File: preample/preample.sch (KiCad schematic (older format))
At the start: 78 parts, among them J1 Conn_01x03, U1 TPS7A39, U2 OP2228UA, U3 OPA228UA, U4 OP2228UA, U5 OPA228UA

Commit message: changed op amps. changed rail voltages. hooked up bypass caps for op amps. additional passives for noise reduction in op amp circuits.
separated the signal grounds. Need to do more research on if that is a
normal thing. Added rca inputs, need to investigate if a simple switch
is enough or if analog mux circuits are needed.
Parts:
- removed C? (x4): 10uF, symbol Device:C_Small
- removed GND? (x4): GND, symbol power:GND
- added AUXGND?: GNDREF, symbol power:GNDREF
- added C17, C18, C?: 100nF, symbol Device:C_Small
- added C24, C35: 10uF, symbol Device:C_Small
- added C26: 10UF, symbol Device:C_Small
- added C27: 20uF, symbol Device:C_Small
- added GND? (x11): GND, symbol power:GND
- added J2: Conn_01x07, symbol Connector_Generic:Conn_01x07
- added J3, J4, J5, J6: Barrel_Jack, symbol Connector:Barrel_Jack
- added R22, R23: 1K, symbol Device:R_Small_US
- added R?: 100R, symbol Device:R_Small_US
- added RV2, RV3: 100K, symbol Device:R_POT_TRIM
- added S1, S2, S4: 4PDT_Switch, symbol preample:4PDT_Switch
- C19, C21, C22: renamed from C?; value 10uF -> 100nF
- R10, R11, R12, R16, R17, R18, R19, R9: value 5K6 -> 560R
- R15, R8: value 5K6 -> 1K
- R3: value 90K9 -> 132K9
- R5: value 100K8 -> 142K9
- RV1: value R_POT_Dual_Separate -> 50K
- U2, U4: value OP2228UA -> OPA2134UA
- U2, U4: value OP2228UA -> OPA2134UA; symbol preample:OP2228UA -> preample:OP2134UA
- U3, U5: value OPA228UA -> OPA134UA; symbol preample:OPA228UA -> preample:OPA134
- renumbered C18 to C20
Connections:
- net labels added: +17V, -17V, AUDIO_A_1_GND, AUDIO_A_1_IN, AUDIO_A_2_GND, AUDIO_A_2_IN, AUDIO_B_1_GND, AUDIO_B_1_IN, AUDIO_B_2_GND, AUDIO_B_2_IN, SIGNAL_GROUND_1, SIGNAL_GROUND_2, TRIM_1A, TRIM_1B, TRIM_2A, TRIM_2B
- net labels removed: +12V, -12V, SIGNAL_GROUND
- wire segments 160 -> 231
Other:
- note added: "1.0"
- note added: "April 2019"
- note added: "DC OFFSET TRIMMERS"
- note added: "INPUT A"
- note added: "INPUT B"
- note added: "OP AMP BYPASS CAPACITORS"
- note added: "OUTPUT TO POWER AMP"
- note added: "Preample preamp"
- note added: "UNREGULATED POWER IN"
- moved on the sheet: C10, C11, C13, C16, C17, C19, C20, C21, C22, C3, C4, C5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

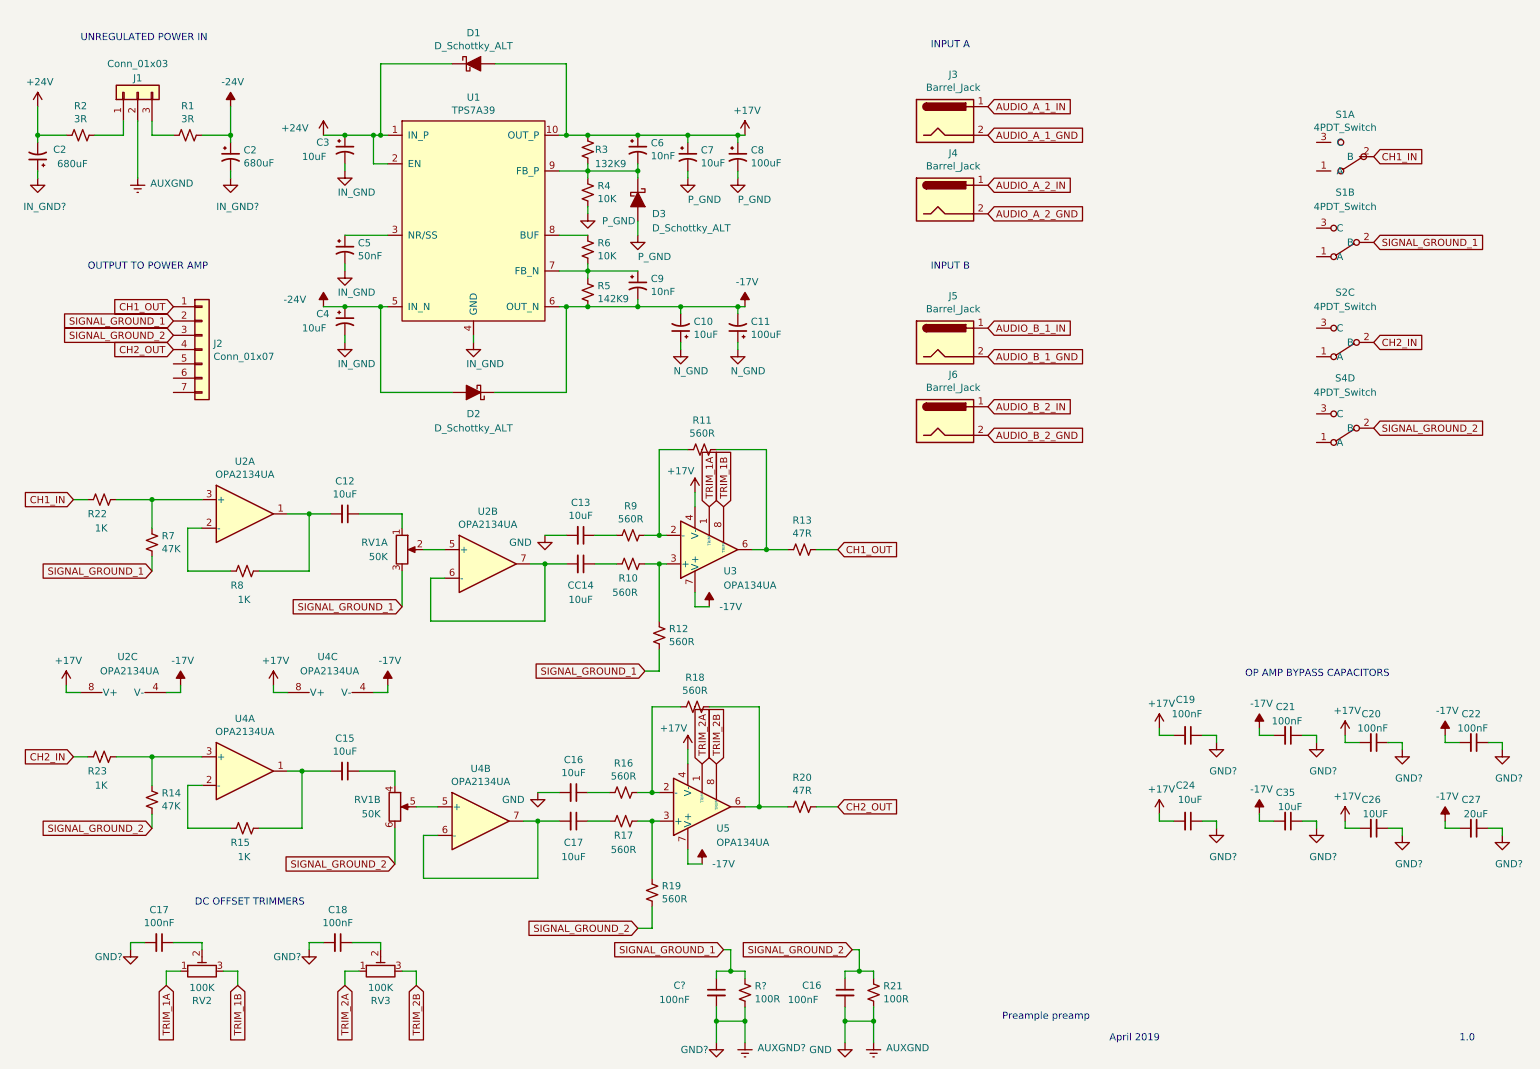
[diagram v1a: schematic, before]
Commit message: added layout sketch. working on grounds. playing with connectors.
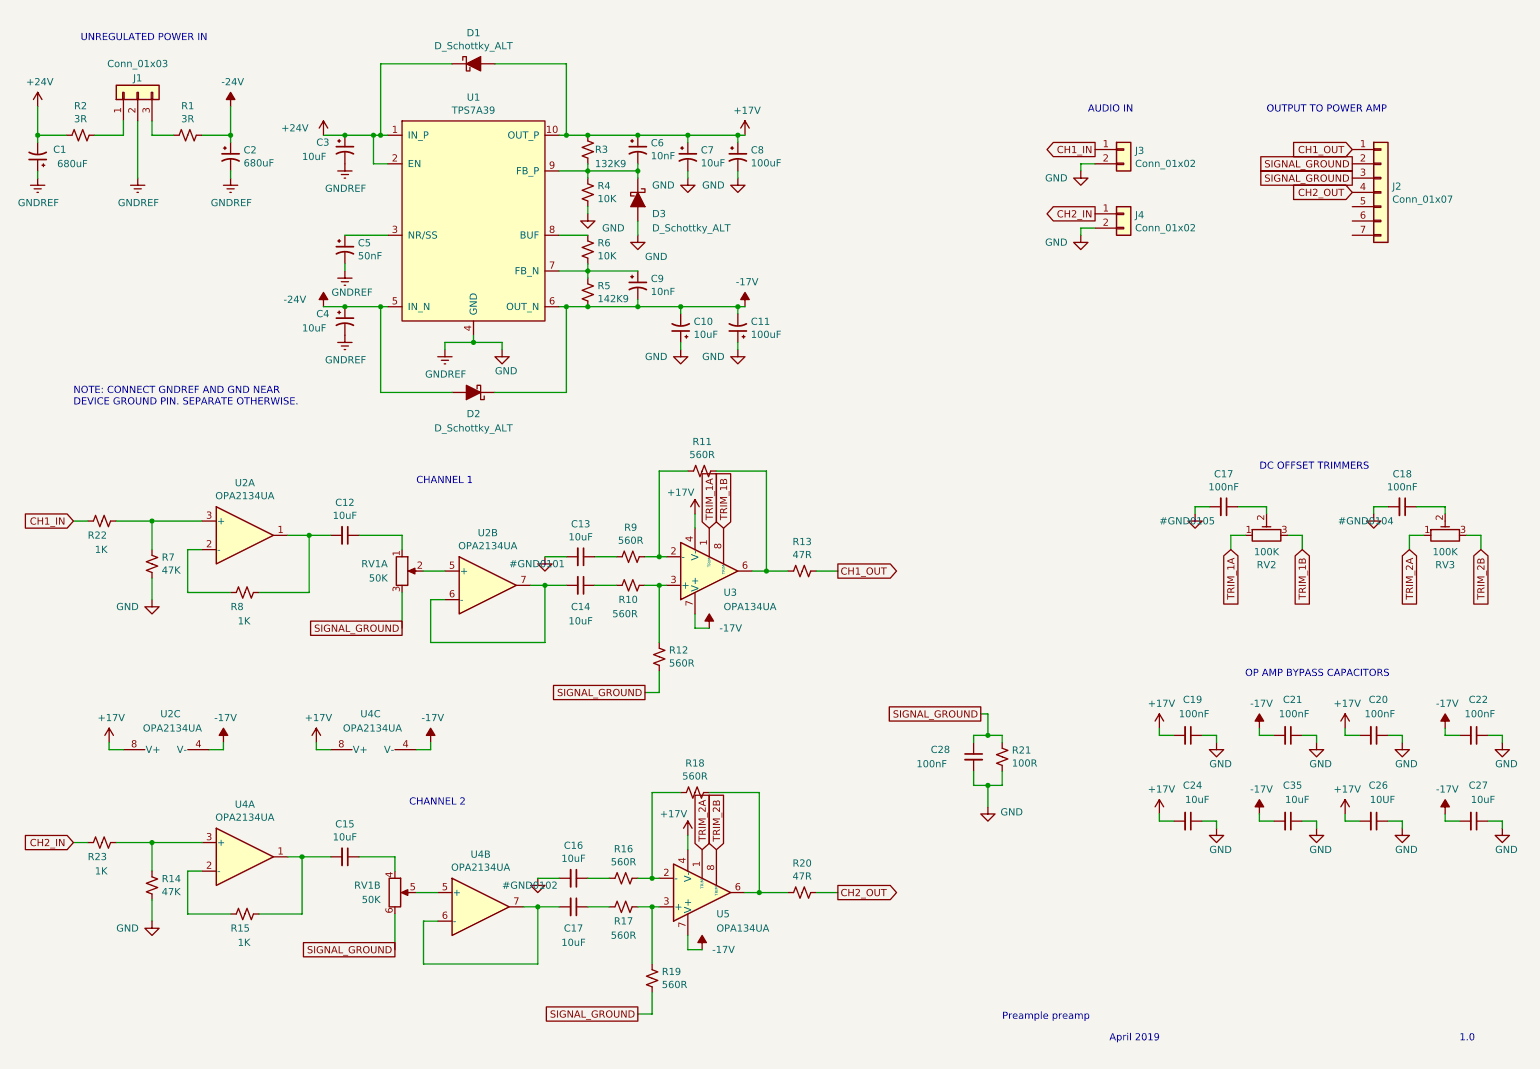
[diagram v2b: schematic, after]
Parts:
- removed AUXGND (x2), AUXGND?: GNDREF, symbol power:GNDREF
- removed C?: 100nF, symbol Device:C_Small
- removed GND (x3), GND? (x11), IN_GND (x4), IN_GND? (x2), N_GND (x2), P_GND (x4): GND, symbol power:GND
- removed J3, J4, J5, J6: Barrel_Jack, symbol Connector:Barrel_Jack
- removed R?: 100R, symbol Device:R_Small_US
- removed S1, S2, S4: 4PDT_Switch, symbol preample:4PDT_Switch
- added J3, J4: Conn_01x02, symbol Connector_Generic:Conn_01x02
- C27: value 20uF -> 10uF
- renumbered C2 to C1, CC14 to C14, C16 to C28
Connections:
- net CH1_IN: now also J3.1 (Pin_1)
- net CH2_IN: now also J4.1 (Pin_1)
- net GND: now also R14.1, R7.1, J3.2 (Pin_2), J4.2 (Pin_2)
- net SIGNAL_GROUND_1 renamed SIGNAL_GROUND
- net SIGNAL_GROUND: now also C28.1, J2.3 (Pin_3), R19.1, R21.1, RV1.6; no longer R7.1
- removed net SIGNAL_GROUND_2: C28.1, J2.3 (Pin_3), R14.1, R19.1, R21.1, RV1.6
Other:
- note added: "AUDIO IN"
- note added: "CHANNEL 1"
- note added: "CHANNEL 2"
- note added: "NOTE: CONNECT GNDREF AND GND NEAR \nDEVICE GROUND PIN. SEPARATE OTHERWISE."
- note removed: "INPUT A"
- note removed: "INPUT B"
- moved on the sheet: C12, C13, C14, C15, C16, C17, C18, C20, C22, C26, C27, C28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

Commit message: Added switching circuit. Added power supply footprints. Started power supply layout.
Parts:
- removed J3, J4: Conn_01x02, symbol Connector_Generic:Conn_01x02
- added C29: 100nF, symbol Device:C_Small
- added J3: Conn_01x06, symbol Connector_Generic:Conn_01x06
- added SW1: SW_DPDT_x2, preample:PBH2UEENAGX, symbol Switch:SW_DPDT_x2
- C1, C2: footprint (none) -> preample:EEV-FK1H681M; Part No (none) -> EEV-FK1H681M
- C10, C3, C4, C7: footprint (none) -> preample:50SVPF10M; Part No (none) -> 50SVPF10M
- C11, C8: footprint (none) -> preample:PCR1E101MCL1GS; Part No (none) -> PCR1E101MCL1GS
- C5: value 50nF -> 47nF; footprint (none) -> Capacitor_SMD:C_0402_1005Metric; Part No (none) -> GRM155R71E473KA88D
- C6, C9: footprint (none) -> Capacitor_SMD:C_0402_1005Metric; Part No (none) -> CL05B103KB5NNNC
- D1, D2, D3: footprint (none) -> Diode_SMD:D_SOD-323F; Part No (none) -> RB751V-40WS RRG
- R1, R2: footprint (none) -> Resistor_SMD:R_0805_2012Metric; Part No (none) -> ERJ-6DQF3R3V
- R3: footprint (none) -> Resistor_SMD:R_0402_1005Metric; Part No (none) -> ERJ-2RKF1333X
- R4, R6: footprint (none) -> Resistor_SMD:R_0402_1005Metric; Part No (none) -> ERJ-2RKF1002X
- R5: footprint (none) -> Resistor_SMD:R_0402_1005Metric; Part No (none) -> ERJ-2RKF1433X
- RV1: value 50K -> 10K; footprint (none) -> preample:RK271 10KAX2
- U1: footprint (none) -> preample:TPS7A39
- U2, U3, U4, U5: footprint (none) -> Package_SO:SOIC-8_3.9x4.9mm_P1.27mm
- renumbered C17 to C15, C15 to C16, C16 to C17, C17 to C18, C18 to C19, C19 to C23, C35 to C25
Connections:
- net CH1_IN: now also SW1.2 (B)
- net CH2_IN: now also SW1.5 (B)
- net GND: now also C29.1
- new net INPUT_A_CH1: J3.6 (Pin_6), SW1.3 (C)
- new net INPUT_A_CH2: J3.5 (Pin_5), SW1.6 (C)
- new net INPUT_B_CH1: J3.2 (Pin_2), SW1.1 (A)
- new net INPUT_B_CH2: J3.1 (Pin_1), SW1.4 (A)
- new net INPUT_GND: C29.2, J3.3 (Pin_3), J3.4 (Pin_4)
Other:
- moved on the sheet: C15, C19, C28, J2, R21, RV2, RV3

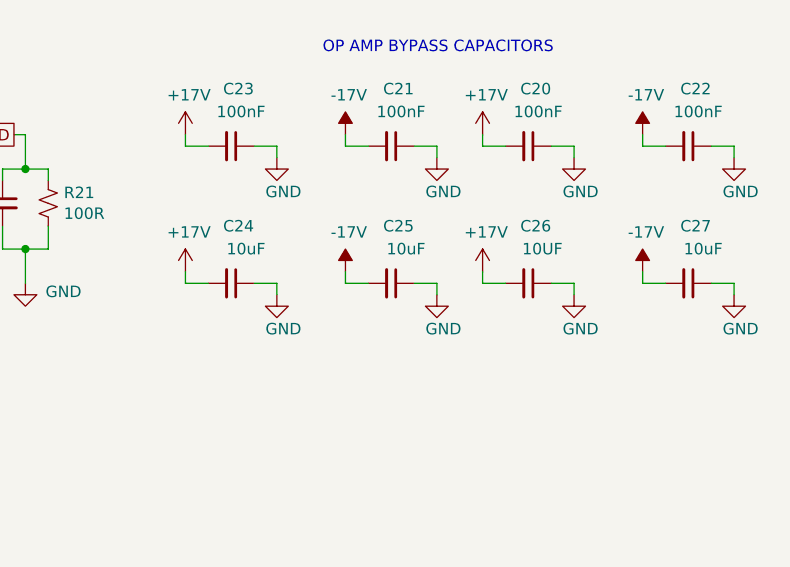
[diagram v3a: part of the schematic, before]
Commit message: swapped 10uF psu caps for smaller ceramics. assigned footprints to many passives. more pcb layout.
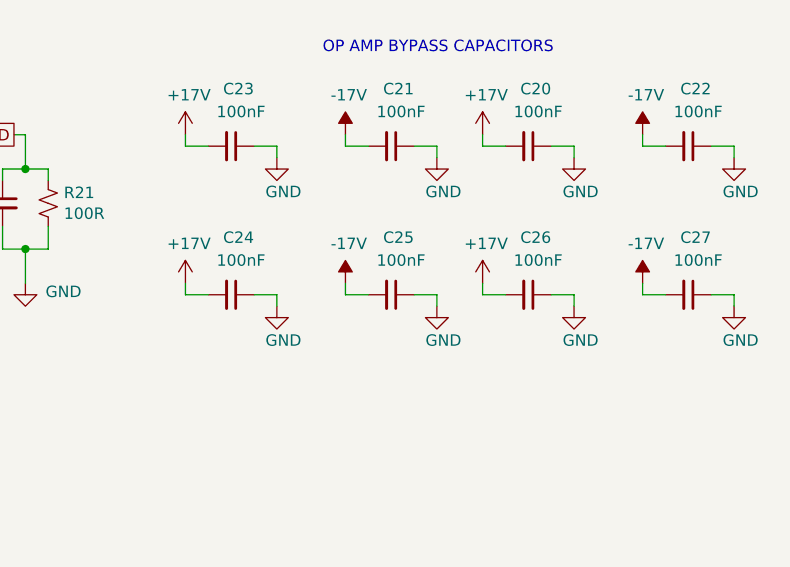
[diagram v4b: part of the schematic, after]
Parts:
- C10, C3, C4, C7: footprint preample:50SVPF10M -> Capacitor_SMD:C_1206_3216Metric; Part No 50SVPF10M -> CL31B106KBHNNNE
- C12, C13, C14, C16, C17, C18: footprint (none) -> preample:MKS2B051001N00JSSD; Part No (none) -> MKS2B051001N00JSSD
- C20, C21, C22, C23, C28: footprint (none) -> Capacitor_SMD:C_0603_1608Metric; Part No (none) -> CL10B104KB8NNNC
- C24, C25, C27: value 10uF -> 100nF; footprint (none) -> Capacitor_SMD:C_0603_1608Metric; Part No (none) -> CL10B104KB8NNNC
- C26: value 10UF -> 100nF; footprint (none) -> Capacitor_SMD:C_0603_1608Metric; Part No (none) -> CL10B104KB8NNNC
- C29: Part No (none) -> SMDTD03100TA00KQ00
- R10, R11, R12, R13, R14, R15, R16, R17, R18, R19, R20, R21, R22, R23, R7, R8, R9: footprint (none) -> Resistor_SMD:R_0402_1005Metric

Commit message: all footprints made except connectors. all signal traced laid.
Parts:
- C15, C19: footprint (none) -> Capacitor_SMD:C_0603_1608Metric; Part No (none) -> CL10B104KB8NNNC
- C28: footprint Capacitor_SMD:C_0603_1608Metric -> preample:SMDTD03100TA00KQ00; Part No CL10B104KB8NNNC -> SMDTD03100TA00KQ00
- C29: footprint (none) -> preample:SMDTD03100TA00KQ00
- RV2, RV3: footprint (none) -> preample:22AR100KLFTR; Part No (none) -> 22AR100KLFTR
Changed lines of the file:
@@
 F 0 "C28" H 7400 5800 50  0000 L CNN
 F 1 "100nF" H 7300 5700 50  0000 L CNN
-F 2 "Capacitor_SMD:C_0603_1608Metric" H 7700 5750 50  0001 C CNN
+F 2 "preample:SMDTD03100TA00KQ00" H 7700 5750 50  0001 C CNN
 F 3 "~" H 7700 5750 50  0001 C CNN
-F 4 "CL10B104KB8NNNC" H 7700 5750 50  0001 C CNN "Part No"
+F 4 "SMDTD03100TA00KQ00" H 7700 5750 50  0001 C CNN "Part No"
 	1    7700 5750
 	1    0    0    -1
@@
 TRIM_2B
 $Comp
-L Device:R_POT_TRIM RV2
-U 1 1 5CC27BD9
-P 9250 4300
-F 0 "RV2" V 9043 4300 50  0000 C CNN
-F 1 "100K" V 9134 4300 50  0000 C CNN
-F 2 "" H 9250 4300 50  0001 C CNN
-F 3 "~" H 9250 4300 50  0001 C CNN
-	1    9250 4300
-	0    -1   -1   0
-$EndComp
-$Comp
 L Device:R_POT_TRIM RV3
 U 1 1 5CC29FE4
@@
 F 0 "RV3" V 10293 4300 50  0000 C CNN
 F 1 "100K" V 10384 4300 50  0000 C CNN
-F 2 "" H 10500 4300 50  0001 C CNN
+F 2 "preample:22AR100KLFTR" H 10500 4300 50  0001 C CNN
 F 3 "~" H 10500 4300 50  0001 C CNN
+F 4 "22AR100KLFTR" V 10500 4300 50  0001 C CNN "Part No"
 	1    10500 4300
 	0    -1   -1   0
-$EndComp
-$Comp
-L Device:C_Small C15
-U 1 1 5CC31E42
-P 8950 4100
-F 0 "C15" V 8721 4100 50  0000 C CNN
-F 1 "100nF" V 8812 4100 50  0000 C CNN
-F 2 "" H 8950 4100 50  0001 C CNN
-F 3 "~" H 8950 4100 50  0001 C CNN
-	1    8950 4100
-	0    1    1    0
 $EndComp
 $Comp
@@
 F 0 "C19" V 9971 4100 50  0000 C CNN
 F 1 "100nF" V 10062 4100 50  0000 C CNN
-F 2 "" H 10200 4100 50  0001 C CNN
+F 2 "Capacitor_SMD:C_0603_1608Metric" H 10200 4100 50  0001 C CNN
 F 3 "~" H 10200 4100 50  0001 C CNN
+F 4 "CL10B104KB8NNNC" V 10200 4100 50  0001 C CNN "Part No"
 	1    10200 4100
 	0    1    1    0
@@
 F 0 "C29" H 10550 1400 50  0000 R CNN
 F 1 "100nF" H 10600 1300 50  0000 R CNN
-F 2 "" H 10700 1350 50  0001 C CNN
+F 2 "preample:SMDTD03100TA00KQ00" H 10700 1350 50  0001 C CNN
 F 3 "~" H 10700 1350 50  0001 C CNN
 F 4 "SMDTD03100TA00KQ00" H 10700 1350 50  0001 C CNN "Part No"
@@
 Wire Wire Line
 	9200 6100 9200 6150
+$Comp
+L Device:C_Small C15
+U 1 1 5CC31E42
+P 8950 4100
+F 0 "C15" V 8721 4100 50  0000 C CNN
+F 1 "100nF" V 8812 4100 50  0000 C CNN
+F 2 "Capacitor_SMD:C_0603_1608Metric" H 8950 4100 50  0001 C CNN
+F 3 "~" H 8950 4100 50  0001 C CNN
+F 4 "CL10B104KB8NNNC" V 8950 4100 50  0001 C CNN "Part No"
+	1    8950 4100
+	0    1    1    0
+$EndComp
+$Comp
+L Device:R_POT_TRIM RV2
+U 1 1 5CC27BD9
+P 9250 4300
+F 0 "RV2" V 9043 4300 50  0000 C CNN
+F 1 "100K" V 9134 4300 50  0000 C CNN
+F 2 "preample:22AR100KLFTR" H 9250 4300 50  0001 C CNN
+F 3 "~" H 9250 4300 50  0001 C CNN
+F 4 "22AR100KLFTR" V 9250 4300 50  0001 C CNN "Part No"
+	1    9250 4300
+	0    -1   -1   0
+$EndComp
 $EndSCHEMATC
